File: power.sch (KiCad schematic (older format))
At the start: 32 parts, among them SW1 SW_DPST_x2, U1 SPX3819-1.8, U2 IMP811REUS-T, U3 SP6205EM5-L-3-3_TR, U4 MP1469GJ

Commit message: finished scimatic for now, and started populating PCB. *chugs rrum*
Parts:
- C1, C10, C11, C12, C13, C14, C15, C2, C3, C4, C5, C6, C7, C8, C9: footprint (none) -> Capacitor_SMD:C_0402_1005Metric
- L1, L2: footprint (none) -> Inductor_SMD:L_0402_1005Metric
- R1, R2, R3, R4, R5, R6, R7, R8, R9: footprint (none) -> Resistor_SMD:R_0402_1005Metric
- SW1, U2: footprint (none) -> Package_TO_SOT_SMD:SOT-543
- U1: footprint (none) -> Package_TO_SOT_SMD:SOT-23-5
- U4: footprint (none) -> Package_TO_SOT_SMD:SOT-223-6
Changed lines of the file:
@@
 $Descr A4 11693 8268
 encoding utf-8
-Sheet 2 4
+Sheet 2 5
 Title ""
 Date ""
@@
 F 0 "R3" V 3743 2350 50  0000 C CNN
 F 1 "100k" V 3834 2350 50  0000 C CNN
-F 2 "" V 3880 2350 50  0001 C CNN
+F 2 "Resistor_SMD:R_0402_1005Metric" V 3880 2350 50  0001 C CNN
 F 3 "~" H 3950 2350 50  0001 C CNN
 	1    3950 2350
@@
 F 0 "C10" H 5915 1946 50  0000 L CNN
 F 1 "10nF" H 5915 1855 50  0000 L CNN
-F 2 "" H 5838 1750 50  0001 C CNN
+F 2 "Capacitor_SMD:C_0402_1005Metric" H 5838 1750 50  0001 C CNN
 F 3 "~" H 5800 1900 50  0001 C CNN
 	1    5800 1900
@@
 F 0 "C9" H 5515 1946 50  0000 L CNN
 F 1 "10nF" H 5515 1855 50  0000 L CNN
-F 2 "" H 5438 1750 50  0001 C CNN
+F 2 "Capacitor_SMD:C_0402_1005Metric" H 5438 1750 50  0001 C CNN
 F 3 "~" H 5400 1900 50  0001 C CNN
 	1    5400 1900
@@
 F 0 "C2" H 2565 1946 50  0000 L CNN
 F 1 "C" H 2565 1855 50  0000 L CNN
-F 2 "" H 2488 1750 50  0001 C CNN
+F 2 "Capacitor_SMD:C_0402_1005Metric" H 2488 1750 50  0001 C CNN
 F 3 "~" H 2450 1900 50  0001 C CNN
 	1    2450 1900
@@
 F 0 "R6" V 7993 1550 50  0000 C CNN
 F 1 "33R" V 8084 1550 50  0000 C CNN
-F 2 "" V 8130 1550 50  0001 C CNN
+F 2 "Resistor_SMD:R_0402_1005Metric" V 8130 1550 50  0001 C CNN
 F 3 "~" H 8200 1550 50  0001 C CNN
 	1    8200 1550
@@
 F 0 "R9" H 8570 1796 50  0000 L CNN
 F 1 "1K" H 8570 1705 50  0000 L CNN
-F 2 "" V 8430 1750 50  0001 C CNN
+F 2 "Resistor_SMD:R_0402_1005Metric" V 8430 1750 50  0001 C CNN
 F 3 "~" H 8500 1750 50  0001 C CNN
 	1    8500 1750
@@
 F 0 "C13" H 8965 1796 50  0000 L CNN
 F 1 "10uF" H 8965 1705 50  0000 L CNN
-F 2 "" H 8888 1600 50  0001 C CNN
+F 2 "Capacitor_SMD:C_0402_1005Metric" H 8888 1600 50  0001 C CNN
 F 3 "~" H 8850 1750 50  0001 C CNN
 	1    8850 1750
@@
 F 0 "C1" H 1065 3846 50  0000 L CNN
 F 1 "100nF" H 1065 3755 50  0000 L CNN
-F 2 "" H 988 3650 50  0001 C CNN
+F 2 "Capacitor_SMD:C_0402_1005Metric" H 988 3650 50  0001 C CNN
 F 3 "~" H 950 3800 50  0001 C CNN
 	1    950  3800
@@
 F 0 "R1" V 1343 3800 50  0000 C CNN
 F 1 "100K" V 1434 3800 50  0000 C CNN
-F 2 "" V 1480 3800 50  0001 C CNN
+F 2 "Resistor_SMD:R_0402_1005Metric" V 1480 3800 50  0001 C CNN
 F 3 "~" H 1550 3800 50  0001 C CNN
 	1    1550 3800
@@
 F 0 "C3" H 3115 3996 50  0000 L CNN
 F 1 "10nF" H 3115 3905 50  0000 L CNN
-F 2 "" H 3038 3800 50  0001 C CNN
+F 2 "Capacitor_SMD:C_0402_1005Metric" H 3038 3800 50  0001 C CNN
 F 3 "~" H 3000 3950 50  0001 C CNN
 	1    3000 3950
@@
 F 0 "C5" H 3565 3996 50  0000 L CNN
 F 1 "100nF" H 3565 3905 50  0000 L CNN
-F 2 "" H 3488 3800 50  0001 C CNN
+F 2 "Capacitor_SMD:C_0402_1005Metric" H 3488 3800 50  0001 C CNN
 F 3 "~" H 3450 3950 50  0001 C CNN
 	1    3450 3950
@@
 F 0 "C6" H 4065 3996 50  0000 L CNN
 F 1 "10uF" H 4065 3905 50  0000 L CNN
-F 2 "" H 3988 3800 50  0001 C CNN
+F 2 "Capacitor_SMD:C_0402_1005Metric" H 3988 3800 50  0001 C CNN
 F 3 "~" H 3950 3950 50  0001 C CNN
 	1    3950 3950
@@
 F 0 "C7" H 5065 3946 50  0000 L CNN
 F 1 "22uF" H 5065 3855 50  0000 L CNN
-F 2 "" H 4950 3900 50  0001 C CNN
+F 2 "Capacitor_SMD:C_0402_1005Metric" H 4950 3900 50  0001 C CNN
 F 3 "~" H 4950 3900 50  0001 C CNN
 	1    4950 3900
@@
 F 0 "C8" H 5465 3946 50  0000 L CNN
 F 1 "100nF" H 5465 3855 50  0000 L CNN
-F 2 "" H 5388 3750 50  0001 C CNN
+F 2 "Capacitor_SMD:C_0402_1005Metric" H 5388 3750 50  0001 C CNN
 F 3 "~" H 5350 3900 50  0001 C CNN
 	1    5350 3900
@@
 F 0 "R4" V 5743 3850 50  0000 C CNN
 F 1 "100K" V 5834 3850 50  0000 C CNN
-F 2 "" V 5880 3850 50  0001 C CNN
+F 2 "Resistor_SMD:R_0402_1005Metric" V 5880 3850 50  0001 C CNN
 F 3 "~" H 5950 3850 50  0001 C CNN
 	1    5950 3850
@@
 F 0 "C11" V 7148 3650 50  0000 C CNN
 F 1 "1uF" V 7239 3650 50  0000 C CNN
-F 2 "" H 7438 3500 50  0001 C CNN
+F 2 "Capacitor_SMD:C_0402_1005Metric" H 7438 3500 50  0001 C CNN
 F 3 "~" H 7400 3650 50  0001 C CNN
 	1    7400 3650
@@
 F 0 "L1" V 8006 3604 50  0000 R CNN
 F 1 "3.3uH" V 7950 3750 50  0000 R CNN
-F 2 "" H 8050 3650 50  0001 C CNN
+F 2 "Inductor_SMD:L_0402_1005Metric" H 8050 3650 50  0001 C CNN
 F 3 "~" H 8050 3650 50  0001 C CNN
 	1    8050 3650
@@
 F 0 "R5" V 7443 4150 50  0000 C CNN
 F 1 "100K" V 7534 4150 50  0000 C CNN
-F 2 "" V 7580 4150 50  0001 C CNN
+F 2 "Resistor_SMD:R_0402_1005Metric" V 7580 4150 50  0001 C CNN
 F 3 "~" H 7650 4150 50  0001 C CNN
 	1    7650 4150
@@
 F 0 "R7" H 8280 3904 50  0000 R CNN
 F 1 "20K" H 8280 3995 50  0000 R CNN
-F 2 "" V 8280 3950 50  0001 C CNN
+F 2 "Resistor_SMD:R_0402_1005Metric" V 8280 3950 50  0001 C CNN
 F 3 "~" H 8350 3950 50  0001 C CNN
 	1    8350 3950
@@
 F 0 "R8" H 8280 4304 50  0000 R CNN
 F 1 "47K" H 8280 4395 50  0000 R CNN
-F 2 "" V 8280 4350 50  0001 C CNN
+F 2 "Resistor_SMD:R_0402_1005Metric" V 8280 4350 50  0001 C CNN
 F 3 "~" H 8350 4350 50  0001 C CNN
 	1    8350 4350
@@
 F 0 "C12" H 8915 3946 50  0000 L CNN
 F 1 "22uF" H 8915 3855 50  0000 L CNN
-F 2 "" H 8800 3900 50  0001 C CNN
+F 2 "Capacitor_SMD:C_0402_1005Metric" H 8800 3900 50  0001 C CNN
 F 3 "~" H 8800 3900 50  0001 C CNN
 	1    8800 3900
@@
 F 0 "C14" H 9315 3946 50  0000 L CNN
 F 1 "100nF" H 9315 3855 50  0000 L CNN
-F 2 "" H 9238 3750 50  0001 C CNN
+F 2 "Capacitor_SMD:C_0402_1005Metric" H 9238 3750 50  0001 C CNN
 F 3 "~" H 9200 3900 50  0001 C CNN
 	1    9200 3900
@@
 F 0 "L2" V 9740 3650 50  0000 C CNN
 F 1 "100r" V 9649 3650 50  0000 C CNN
-F 2 "" H 9550 3650 50  0001 C CNN
+F 2 "Inductor_SMD:L_0402_1005Metric" H 9550 3650 50  0001 C CNN
 F 3 "~" H 9550 3650 50  0001 C CNN
 	1    9550 3650
@@
 F 0 "C15" H 9965 3946 50  0000 L CNN
 F 1 "22uF" H 9965 3855 50  0000 L CNN
-F 2 "" H 9850 3900 50  0001 C CNN
+F 2 "Capacitor_SMD:C_0402_1005Metric" H 9850 3900 50  0001 C CNN
 F 3 "~" H 9850 3900 50  0001 C CNN
 	1    9850 3900
@@
 F 0 "R2" H 1820 6196 50  0000 L CNN
 F 1 "100K" H 1820 6105 50  0000 L CNN
-F 2 "" V 1680 6150 50  0001 C CNN
+F 2 "Resistor_SMD:R_0402_1005Metric" V 1680 6150 50  0001 C CNN
 F 3 "~" H 1750 6150 50  0001 C CNN
 	1    1750 6150
@@
 F 0 "C4" V 2998 5700 50  0000 C CNN
 F 1 "100nF" V 3089 5700 50  0000 C CNN
-F 2 "" H 3288 5550 50  0001 C CNN
+F 2 "Capacitor_SMD:C_0402_1005Metric" H 3288 5550 50  0001 C CNN
 F 3 "~" H 3250 5700 50  0001 C CNN
 	1    3250 5700
@@
 F 0 "U2" H 2500 5925 50  0000 C CNN
 F 1 "IMP811REUS-T" H 2500 5834 50  0000 C CNN
-F 2 "" H 2500 5700 50  0001 C CNN
+F 2 "Package_TO_SOT_SMD:SOT-543" H 2500 5700 50  0001 C CNN
 F 3 "" H 2500 5700 50  0001 C CNN
 	1    2500 5700
@@
 F 0 "U1" H 2425 3315 50  0000 C CNN
 F 1 "SPX3819-1.8" H 2425 3224 50  0000 C CNN
-F 2 "" H 2400 3300 50  0001 C CNN
+F 2 "Package_TO_SOT_SMD:SOT-23-5" H 2400 3300 50  0001 C CNN
 F 3 "" H 2400 3300 50  0001 C CNN
 	1    2400 3300
@@
 F 0 "U4" H 6650 3375 50  0000 C CNN
 F 1 "MP1469GJ" H 6650 3284 50  0000 C CNN
-F 2 "" H 6650 3400 50  0001 C CNN
+F 2 "Package_TO_SOT_SMD:SOT-223-6" H 6650 3400 50  0001 C CNN
 F 3 "" H 6650 3400 50  0001 C CNN
 	1    6650 3400
@@
 F 0 "SW1" H 4800 6335 50  0000 C CNN
 F 1 "SW_DPST_x2" H 4800 6244 50  0000 C CNN
-F 2 "" H 4800 6100 50  0001 C CNN
+F 2 "Package_TO_SOT_SMD:SOT-543" H 4800 6100 50  0001 C CNN
 F 3 "~" H 4800 6100 50  0001 C CNN
 	1    4800 6100

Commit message: started layout of the PCB, allso moved onto craken rum, from captin morgan. please for the love of god check the footprints are right. @MAX
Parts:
- SW1: footprint Package_TO_SOT_SMD:SOT-543 -> Jumper:SolderJumper-2_P1.3mm_Open_Pad1.0x1.5mm
- U3: footprint SOT-23-5_VAR-AA -> Package_TO_SOT_SMD:SOT-23-5
- U4: footprint Package_TO_SOT_SMD:SOT-223-6 -> Package_TO_SOT_SMD:SOT-23-6
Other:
- moved on the sheet: C10, C2, C9, R3, U3
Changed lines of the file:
@@
 $EndDescr
 Wire Wire Line
-	3300 1650 2800 1650
-Wire Wire Line
-	2800 1650 2800 2350
-Wire Wire Line
-	5300 2350 5300 1850
-Wire Wire Line
-	5300 1850 5100 1850
-Connection ~ 2800 1650
-Wire Wire Line
-	2800 1650 2450 1650
+	2600 1400 2100 1400
+Wire Wire Line
+	2100 1400 2100 2100
+Wire Wire Line
+	4600 2100 4600 1600
+Wire Wire Line
+	4600 1600 4400 1600
+Connection ~ 2100 1400
+Wire Wire Line
+	2100 1400 1750 1400
 $Comp
 L power:GND #PWR0101
 U 1 1 5F46AF52
-P 3100 1750
-F 0 "#PWR0101" H 3100 1500 50  0001 C CNN
-F 1 "GND" V 3105 1622 50  0000 R CNN
-F 2 "" H 3100 1750 50  0001 C CNN
-F 3 "" H 3100 1750 50  0001 C CNN
-	1    3100 1750
-	1    0    0    -1
-$EndComp
-Wire Wire Line
-	3100 1750 3300 1750
+P 2400 1500
+F 0 "#PWR0101" H 2400 1250 50  0001 C CNN
+F 1 "GND" V 2405 1372 50  0000 R CNN
+F 2 "" H 2400 1500 50  0001 C CNN
+F 3 "" H 2400 1500 50  0001 C CNN
+	1    2400 1500
+	1    0    0    -1
+$EndComp
+Wire Wire Line
+	2400 1500 2600 1500
 $Comp
 L power:+5V #PWR0102
 U 1 1 5F46BAA8
-P 2300 1650
-F 0 "#PWR0102" H 2300 1500 50  0001 C CNN
-F 1 "+5V" V 2315 1778 50  0000 L CNN
-F 2 "" H 2300 1650 50  0001 C CNN
-F 3 "" H 2300 1650 50  0001 C CNN
-	1    2300 1650
+P 1600 1400
+F 0 "#PWR0102" H 1600 1250 50  0001 C CNN
+F 1 "+5V" V 1615 1528 50  0000 L CNN
+F 2 "" H 1600 1400 50  0001 C CNN
+F 3 "" H 1600 1400 50  0001 C CNN
+	1    1600 1400
 	0    -1   -1   0
 $EndComp
@@
 L power:+3.3V #PWR0103
 U 1 1 5F46C36C
-P 5900 1650
-F 0 "#PWR0103" H 5900 1500 50  0001 C CNN
-F 1 "+3.3V" V 5915 1778 50  0000 L CNN
-F 2 "" H 5900 1650 50  0001 C CNN
-F 3 "" H 5900 1650 50  0001 C CNN
-	1    5900 1650
+P 5200 1400
+F 0 "#PWR0103" H 5200 1250 50  0001 C CNN
+F 1 "+3.3V" V 5215 1528 50  0000 L CNN
+F 2 "" H 5200 1400 50  0001 C CNN
+F 3 "" H 5200 1400 50  0001 C CNN
+	1    5200 1400
 	0    1    1    0
 $EndComp
 Wire Wire Line
-	5100 1750 5400 1750
+	4400 1500 4700 1500
 $Comp
 L power:GND #PWR0104
 U 1 1 5F46E6EF
-P 5650 2250
-F 0 "#PWR0104" H 5650 2000 50  0001 C CNN
-F 1 "GND" H 5655 2077 50  0000 C CNN
-F 2 "" H 5650 2250 50  0001 C CNN
-F 3 "" H 5650 2250 50  0001 C CNN
-	1    5650 2250
-	1    0    0    -1
-$EndComp
-Wire Wire Line
-	5650 2050 5650 2250
-Wire Wire Line
-	5800 2050 5650 2050
-Wire Wire Line
-	5800 1750 5800 1650
-Wire Wire Line
-	5800 1650 5900 1650
-Wire Wire Line
-	5800 1650 5100 1650
-Connection ~ 5800 1650
+P 4950 2000
+F 0 "#PWR0104" H 4950 1750 50  0001 C CNN
+F 1 "GND" H 4955 1827 50  0000 C CNN
+F 2 "" H 4950 2000 50  0001 C CNN
+F 3 "" H 4950 2000 50  0001 C CNN
+	1    4950 2000
+	1    0    0    -1
+$EndComp
+Wire Wire Line
+	4950 1800 4950 2000
+Wire Wire Line
+	5100 1800 4950 1800
+Wire Wire Line
+	5100 1500 5100 1400
+Wire Wire Line
+	5100 1400 5200 1400
+Wire Wire Line
+	5100 1400 4400 1400
+Connection ~ 5100 1400
 $Comp
 L Device:R R3
 U 1 1 5F46F847
-P 3950 2350
-F 0 "R3" V 3743 2350 50  0000 C CNN
-F 1 "100k" V 3834 2350 50  0000 C CNN
-F 2 "Resistor_SMD:R_0402_1005Metric" V 3880 2350 50  0001 C CNN
-F 3 "~" H 3950 2350 50  0001 C CNN
-	1    3950 2350
+P 3250 2100
+F 0 "R3" V 3043 2100 50  0000 C CNN
+F 1 "100k" V 3134 2100 50  0000 C CNN
+F 2 "Resistor_SMD:R_0402_1005Metric" V 3180 2100 50  0001 C CNN
+F 3 "~" H 3250 2100 50  0001 C CNN
+	1    3250 2100
 	0    1    1    0
 $EndComp
 Wire Wire Line
-	5300 2350 4100 2350
-Wire Wire Line
-	2800 2350 3800 2350
+	4600 2100 3400 2100
+Wire Wire Line
+	2100 2100 3100 2100
 $Comp
 L Device:C C10
 U 1 1 5F46E13B
-P 5800 1900
-F 0 "C10" H 5915 1946 50  0000 L CNN
-F 1 "10nF" H 5915 1855 50  0000 L CNN
-F 2 "Capacitor_SMD:C_0402_1005Metric" H 5838 1750 50  0001 C CNN
-F 3 "~" H 5800 1900 50  0001 C CNN
-	1    5800 1900
-	1    0    0    -1
-$EndComp
-Connection ~ 5650 2050
+P 5100 1650
+F 0 "C10" H 5215 1696 50  0000 L CNN
+F 1 "10nF" H 5215 1605 50  0000 L CNN
+F 2 "Capacitor_SMD:C_0402_1005Metric" H 5138 1500 50  0001 C CNN
+F 3 "~" H 5100 1650 50  0001 C CNN
+	1    5100 1650
+	1    0    0    -1
+$EndComp
+Connection ~ 4950 1800
 $Comp
 L Device:C C9
 U 1 1 5F46CE59
-P 5400 1900
-F 0 "C9" H 5515 1946 50  0000 L CNN
-F 1 "10nF" H 5515 1855 50  0000 L CNN
-F 2 "Capacitor_SMD:C_0402_1005Metric" H 5438 1750 50  0001 C CNN
-F 3 "~" H 5400 1900 50  0001 C CNN
-	1    5400 1900
-	1    0    0    -1
-$EndComp
-Wire Wire Line
-	5400 2050 5650 2050
+P 4700 1650
+F 0 "C9" H 4815 1696 50  0000 L CNN
+F 1 "10nF" H 4815 1605 50  0000 L CNN
+F 2 "Capacitor_SMD:C_0402_1005Metric" H 4738 1500 50  0001 C CNN
+F 3 "~" H 4700 1650 50  0001 C CNN
+	1    4700 1650
+	1    0    0    -1
+$EndComp
+Wire Wire Line
+	4700 1800 4950 1800
 $Comp
 L power:GND #PWR0105
 U 1 1 5F4AC863
-P 2450 2150
-F 0 "#PWR0105" H 2450 1900 50  0001 C CNN
-F 1 "GND" H 2455 1977 50  0000 C CNN
-F 2 "" H 2450 2150 50  0001 C CNN
-F 3 "" H 2450 2150 50  0001 C CNN
-	1    2450 2150
+P 1750 1900
+F 0 "#PWR0105" H 1750 1650 50  0001 C CNN
+F 1 "GND" H 1755 1727 50  0000 C CNN
+F 2 "" H 1750 1900 50  0001 C CNN
+F 3 "" H 1750 1900 50  0001 C CNN
+	1    1750 1900
 	1    0    0    -1
 $EndComp
@@
 L Device:C C2
 U 1 1 5F4ACF4B
-P 2450 1900
-F 0 "C2" H 2565 1946 50  0000 L CNN
-F 1 "C" H 2565 1855 50  0000 L CNN
-F 2 "Capacitor_SMD:C_0402_1005Metric" H 2488 1750 50  0001 C CNN
-F 3 "~" H 2450 1900 50  0001 C CNN
-	1    2450 1900
+P 1750 1650
+F 0 "C2" H 1865 1696 50  0000 L CNN
+F 1 "C" H 1865 1605 50  0000 L CNN
+F 2 "Capacitor_SMD:C_0402_1005Metric" H 1788 1500 50  0001 C CNN
+F 3 "~" H 1750 1650 50  0001 C CNN
+	1    1750 1650
 	1    0    0    -1
 $EndComp
@@
 L Csky:SP6205EM5-L-3-3_TR U3
 U 1 1 5F4A6E5D
-P 3300 1650
-F 0 "U3" H 4200 2037 60  0000 C CNN
-F 1 "SP6205EM5-L-3-3_TR" H 4200 1931 60  0000 C CNN
-F 2 "SOT-23-5_VAR-AA" H 4200 1890 60  0001 C CNN
-F 3 "" H 3300 1650 60  0000 C CNN
-	1    3300 1650
-	1    0    0    -1
-$EndComp
-Wire Wire Line
-	2450 2150 2450 2050
-Wire Wire Line
-	2450 1750 2450 1650
-Connection ~ 2450 1650
-Wire Wire Line
-	2450 1650 2300 1650
+P 2600 1400
+F 0 "U3" H 3500 1787 60  0000 C CNN
+F 1 "SP6205EM5-L-3-3_TR" H 3500 1681 60  0000 C CNN
+F 2 "Package_TO_SOT_SMD:SOT-23-5" H 3500 1640 60  0001 C CNN
+F 3 "" H 2600 1400 60  0000 C CNN
+	1    2600 1400
+	1    0    0    -1
+$EndComp
+Wire Wire Line
+	1750 1900 1750 1800
+Wire Wire Line
+	1750 1500 1750 1400
+Connection ~ 1750 1400
+Wire Wire Line
+	1750 1400 1600 1400
 Text Notes 9050 1300 0    50   ~ 0
 HDMI\n
-Text Notes 5600 1200 0    50   ~ 0
+Text Notes 4900 950  0    50   ~ 0
 ICE\nIO
 $Comp
@@
 F 0 "U4" H 6650 3375 50  0000 C CNN
 F 1 "MP1469GJ" H 6650 3284 50  0000 C CNN
-F 2 "Package_TO_SOT_SMD:SOT-223-6" H 6650 3400 50  0001 C CNN
+F 2 "Package_TO_SOT_SMD:SOT-23-6" H 6650 3400 50  0001 C CNN
 F 3 "" H 6650 3400 50  0001 C CNN
 	1    6650 3400
@@
 F 0 "SW1" H 4800 6335 50  0000 C CNN
 F 1 "SW_DPST_x2" H 4800 6244 50  0000 C CNN
-F 2 "Package_TO_SOT_SMD:SOT-543" H 4800 6100 50  0001 C CNN
+F 2 "Jumper:SolderJumper-2_P1.3mm_Open_Pad1.0x1.5mm" H 4800 6100 50  0001 C CNN
 F 3 "~" H 4800 6100 50  0001 C CNN
 	1    4800 6100

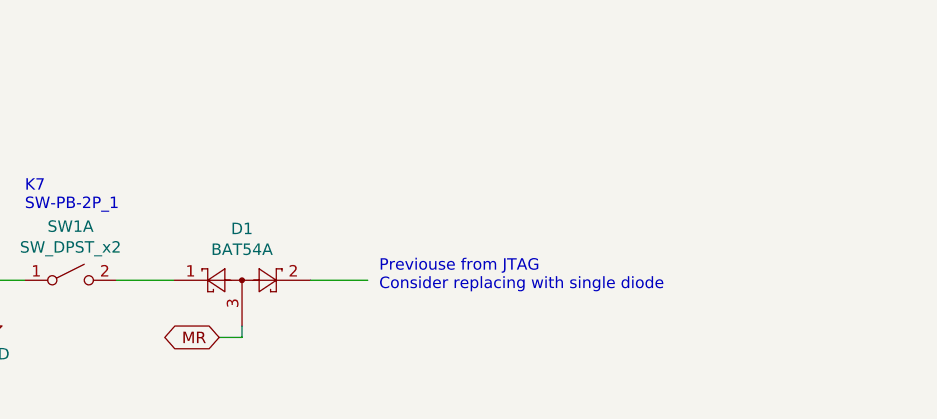
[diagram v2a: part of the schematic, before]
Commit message: started some routing, removed some useless components
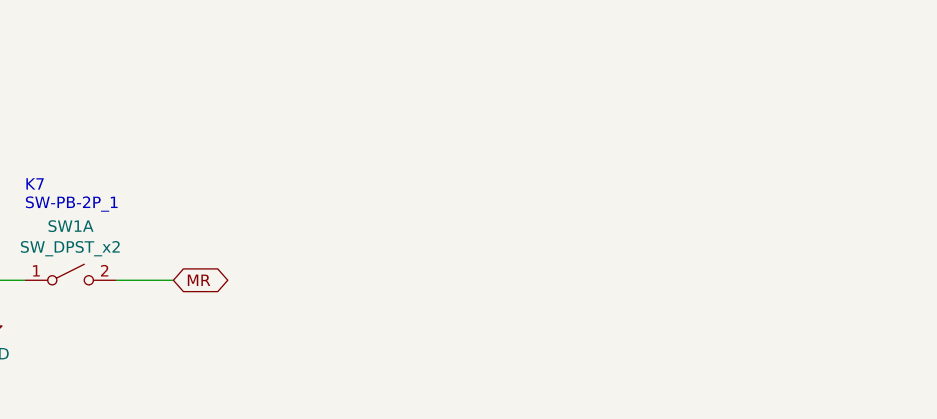
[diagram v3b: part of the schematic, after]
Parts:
- removed D1: BAT54A, Package_TO_SOT_SMD:SOT-23, symbol Diode:BAT54A
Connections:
- net MR: now also SW1.2 (B)
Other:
- note removed: "Previouse from JTAG\nConsider replacing with single diode"
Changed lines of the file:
@@
 Wire Wire Line
 	5700 3650 6200 3650
-$Comp
-L Diode:BAT54A D1
-U 1 1 5F4AB793
-P 5550 6100
-F 0 "D1" H 5550 6325 50  0000 C CNN
-F 1 "BAT54A" H 5550 6234 50  0000 C CNN
-F 2 "Package_TO_SOT_SMD:SOT-23" H 5625 6225 50  0001 L CNN
-F 3 "http://www.diodes.com/_files/datasheets/ds11005.pdf" H 5430 6100 50  0001 C CNN
-	1    5550 6100
-	1    0    0    -1
-$EndComp
-Text GLabel 5450 6350 0    50   BiDi ~ 0
+Text GLabel 5250 6100 2    50   BiDi ~ 0
 MR
-Wire Wire Line
-	5450 6350 5550 6350
-Wire Wire Line
-	5550 6350 5550 6300
-Wire Wire Line
-	5850 6100 6100 6100
 $Comp
 L Switch:SW_DPST_x2 SW1
@@
 Text Notes 4600 5800 0    50   ~ 0
 K7\nSW-PB-2P_1\n
-Text Notes 6150 6150 0    50   ~ 0
-Previouse from JTAG\nConsider replacing with single diode
 $Comp
 L power:+3.3V #PWR0124

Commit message: added power allé, and did more routing
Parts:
- U2: footprint Package_TO_SOT_SMD:SOT-543 -> Package_TO_SOT_SMD:SOT-143
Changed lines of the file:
@@
 F 0 "U2" H 2500 5925 50  0000 C CNN
 F 1 "IMP811REUS-T" H 2500 5834 50  0000 C CNN
-F 2 "Package_TO_SOT_SMD:SOT-543" H 2500 5700 50  0001 C CNN
+F 2 "Package_TO_SOT_SMD:SOT-143" H 2500 5700 50  0001 C CNN
 F 3 "" H 2500 5700 50  0001 C CNN
 	1    2500 5700
